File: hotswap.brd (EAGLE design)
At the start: 160 x 100 mm, 10 parts, among them U1 LTC4416EMS#PBF, U2 641737-1, U3 641737-1, U4 641737-1

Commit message: Hotswap Design Review (Asha)
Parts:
- U2: value 641737-1 -> WALL
- U3: value 641737-1 -> BATTERY
- U4: value 641737-1 -> COMPUTER
- moved R2E 5.08 mm to (25.4, 29.2)
- moved R2A 2.54 mm to (26.7, 34.3)
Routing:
- net N$9: track 15.1 -> 7.55 mm
- net N$2: track 15.8 -> 9.46 mm
- net VCC_WALL: track 21.7 -> 18.9 mm
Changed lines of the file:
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@@
 </autorouter>
 <elements>
-<element name="R2A" library="rcl" library_urn="urn:adsk.eagle:library:334" package="R0603" package3d_urn="urn:adsk.eagle:package:23555/2" value="158k" x="24.13" y="34.29" smashed="yes" rot="R90">
-<attribute name="NAME" x="23.495" y="33.655" size="1.27" layer="25" rot="R90"/>
-<attribute name="SPICEPREFIX" value="R" x="153.67" y="69.85" size="1.778" layer="27" rot="R90" display="off"/>
-<attribute name="VALUE" x="26.035" y="33.655" size="1.27" layer="27" rot="R90"/>
+<element name="R2A" library="rcl" library_urn="urn:adsk.eagle:library:334" package="R0603" package3d_urn="urn:adsk.eagle:package:23555/2" value="158k" x="26.67" y="34.29" smashed="yes" rot="R90">
+<attribute name="NAME" x="26.035" y="33.655" size="1.27" layer="25" rot="R90"/>
+<attribute name="SPICEPREFIX" value="R" x="156.21" y="69.85" size="1.778" layer="27" rot="R90" display="off"/>
+<attribute name="VALUE" x="28.575" y="33.655" size="1.27" layer="27" rot="R90"/>
 </element>
 <element name="R2C" library="rcl" library_urn="urn:adsk.eagle:library:334" package="R0603" package3d_urn="urn:adsk.eagle:package:23555/2" value="11.5k" x="27.94" y="29.21" smashed="yes" rot="R90">
@@
 <attribute name="VALUE" x="29.845" y="28.575" size="1.27" layer="27" rot="R90"/>
 </element>
-<element name="R2E" library="rcl" library_urn="urn:adsk.eagle:library:334" package="R0603" package3d_urn="urn:adsk.eagle:package:23555/2" value="105k" x="20.32" y="29.21" smashed="yes" rot="R90">
-<attribute name="NAME" x="19.685" y="28.575" size="1.27" layer="25" rot="R90"/>
-<attribute name="SPICEPREFIX" value="R" x="149.86" y="71.12" size="1.778" layer="27" rot="R90" display="off"/>
-<attribute name="VALUE" x="22.225" y="28.575" size="1.27" layer="27" rot="R90"/>
+<element name="R2E" library="rcl" library_urn="urn:adsk.eagle:library:334" package="R0603" package3d_urn="urn:adsk.eagle:package:23555/2" value="105k" x="25.4" y="29.21" smashed="yes" rot="R90">
+<attribute name="NAME" x="24.765" y="28.575" size="1.27" layer="25" rot="R90"/>
+<attribute name="SPICEPREFIX" value="R" x="154.94" y="71.12" size="1.778" layer="27" rot="R90" display="off"/>
+<attribute name="VALUE" x="27.305" y="28.575" size="1.27" layer="27" rot="R90"/>
 </element>
 <element name="U$3" library="IGVC-Discrete" package="DPACK_2" value="SUP75P03_07" x="31.75" y="43.18" smashed="yes" rot="R270">
@@
 <attribute name="VALUE" x="30.1371" y="28.639540625" size="0.4" layer="27" align="top-left"/>
 </element>
-<element name="U2" library="IGVC-Connector" package="641737-1" value="641737-1" x="13.97" y="35.56" smashed="yes" rot="R270">
+<element name="U2" library="IGVC-Connector" package="641737-1" value="WALL" x="13.97" y="35.56" smashed="yes" rot="R270">
 <attribute name="MANUFACTURER_PART_NUMBER" value="6417371" x="-16.51" y="10.16" size="1.778" layer="27" rot="R270" display="off"/>
 <attribute name="NAME" x="13.335" y="46.4566" size="1.27" layer="25" ratio="6" rot="SR270"/>
 <attribute name="VENDOR" value="TE Connectivity" x="-16.51" y="10.16" size="1.778" layer="27" rot="R270" display="off"/>
 </element>
-<element name="U3" library="IGVC-Connector" package="641737-1" value="641737-1" x="13.97" y="8.89" smashed="yes" rot="R270">
+<element name="U3" library="IGVC-Connector" package="641737-1" value="BATTERY" x="13.97" y="8.89" smashed="yes" rot="R270">
 <attribute name="MANUFACTURER_PART_NUMBER" value="6417371" x="-58.42" y="-16.51" size="1.778" layer="27" rot="R270" display="off"/>
 <attribute name="NAME" x="13.335" y="19.7866" size="1.27" layer="25" ratio="6" rot="SR270"/>
 <attribute name="VENDOR" value="TE Connectivity" x="-58.42" y="-16.51" size="1.778" layer="27" rot="R270" display="off"/>
 </element>
-<element name="U4" library="IGVC-Connector" package="641737-1" value="641737-1" x="45.72" y="36.83" smashed="yes" rot="R90">
+<element name="U4" library="IGVC-Connector" package="641737-1" value="COMPUTER" x="45.72" y="36.83" smashed="yes" rot="R90">
 <attribute name="MANUFACTURER_PART_NUMBER" value="6417371" x="160.02" y="62.23" size="1.778" layer="27" rot="R90" display="off"/>
 <attribute name="NAME" x="46.355" y="25.9334" size="1.27" layer="25" ratio="6" rot="SR90"/>
@@
 <contactref element="U1" pad="3"/>
 <contactref element="R2C" pad="1"/>
-<contactref element="U2" pad="3"/>
-<contactref element="U2" pad="4"/>
-<contactref element="U4" pad="3"/>
-<contactref element="U4" pad="4"/>
-<contactref element="U3" pad="3"/>
-<contactref element="U3" pad="4"/>
-<polygon width="0.254" layer="16">
+<polygon width="0.254" layer="16" thermals="no">
 <vertex x="0" y="58.42"/>
 <vertex x="59.69" y="58.42"/>
@@
 <wire x1="32.639" y1="30.48" x2="30.8356" y2="30.48" width="0.254" layer="1"/>
 <via x="33.02" y="30.099" extent="1-16" drill="0.35"/>
+<contactref element="U2" pad="4"/>
+<contactref element="U2" pad="3"/>
+<contactref element="U3" pad="4"/>
+<contactref element="U3" pad="3"/>
+<contactref element="U4" pad="3"/>
+<contactref element="U4" pad="4"/>
 </signal>
 <signal name="N$4">
@@
 <contactref element="U1" pad="5"/>
 <contactref element="R2E" pad="1"/>
-<wire x1="30.8356" y1="29.479240625" x2="29.21" y2="27.853640625" width="0.254" layer="1"/>
-<wire x1="29.21" y1="27.853640625" x2="29.21" y2="26.67" width="0.254" layer="1"/>
-<wire x1="29.21" y1="26.67" x2="27.94" y2="25.4" width="0.254" layer="1"/>
-<wire x1="27.94" y1="25.4" x2="21.59" y2="25.4" width="0.254" layer="1"/>
-<wire x1="21.59" y1="25.4" x2="20.32" y2="26.67" width="0.254" layer="1"/>
-<wire x1="20.32" y1="26.67" x2="20.32" y2="28.36" width="0.254" layer="1"/>
+<wire x1="30.8356" y1="29.479240625" x2="28.026359375" y2="26.67" width="0.254" layer="1"/>
+<wire x1="28.026359375" y1="26.67" x2="26.67" y2="26.67" width="0.254" layer="1"/>
+<wire x1="26.67" y1="26.67" x2="25.4" y2="27.94" width="0.254" layer="1"/>
+<wire x1="25.4" y1="27.94" x2="25.4" y2="28.36" width="0.254" layer="1"/>
 </signal>
 <signal name="N$2">
@@
 <contactref element="R2A" pad="1"/>
 <contactref element="R2C" pad="2"/>
-<wire x1="24.13" y1="33.44" x2="20.75" y2="30.06" width="0.254" layer="1"/>
-<wire x1="20.75" y1="30.06" x2="20.32" y2="30.06" width="0.254" layer="1"/>
+<wire x1="26.67" y1="33.44" x2="26.67" y2="31.33" width="0.254" layer="1"/>
+<wire x1="26.67" y1="31.33" x2="25.4" y2="30.06" width="0.254" layer="1"/>
 <wire x1="30.8356" y1="29.97961875" x2="27.94" y2="29.97961875" width="0.254" layer="1"/>
 <wire x1="27.94" y1="29.97961875" x2="27.94" y2="30.06" width="0.254" layer="1"/>
-<wire x1="20.32" y1="30.06" x2="27.85961875" y2="30.06" width="0.254" layer="1"/>
+<wire x1="25.4" y1="30.06" x2="27.85961875" y2="30.06" width="0.254" layer="1"/>
 <wire x1="27.85961875" y1="30.06" x2="27.94" y2="29.97961875" width="0.254" layer="1"/>
 </signal>
@@
 <contactref element="U2" pad="2"/>
 <contactref element="U2" pad="1"/>
-<polygon width="0.254" layer="1">
+<polygon width="0.254" layer="1" thermals="no">
 <vertex x="1.27" y="57.15"/>
 <vertex x="29.21" y="57.15"/>
@@
 <vertex x="1.27" y="41.91"/>
 </polygon>
-<wire x1="24.13" y1="35.14" x2="28.28961875" y2="30.98038125" width="0.254" layer="1"/>
-<wire x1="28.28961875" y1="30.98038125" x2="30.8356" y2="30.98038125" width="0.254" layer="1"/>
-<wire x1="24.13" y1="35.14" x2="26.95" y2="37.96" width="0.254" layer="1"/>
-<wire x1="26.95" y1="37.96" x2="26.95" y2="40.9" width="0.254" layer="1"/>
+<wire x1="26.67" y1="35.14" x2="26.88" y2="35.35" width="0.254" layer="1"/>
+<wire x1="26.88" y1="35.35" x2="26.95" y2="35.42" width="0.254" layer="1"/>
+<wire x1="26.95" y1="35.42" x2="26.95" y2="40.9" width="0.254" layer="1"/>
 <wire x1="35.2044" y1="30.98038125" x2="36.06038125" y2="30.98038125" width="0.254" layer="1"/>
 <wire x1="36.06038125" y1="30.98038125" x2="36.83" y2="31.75" width="0.254" layer="1"/>
 <via x="36.83" y="31.75" extent="1-16" drill="0.35"/>
-<wire x1="30.8356" y1="30.98038125" x2="35.2044" y2="30.98038125" width="0.254" layer="1"/>
+<wire x1="27.94" y1="32.639" x2="27.94" y2="34.29" width="0.254" layer="1"/>
+<wire x1="27.94" y1="34.29" x2="26.88" y2="35.35" width="0.254" layer="1"/>
+<wire x1="35.2044" y1="30.98038125" x2="30.8356" y2="30.98038125" width="0.254" layer="1"/>
+<wire x1="30.8356" y1="30.98038125" x2="29.59861875" y2="30.98038125" width="0.254" layer="1"/>
+<wire x1="29.59861875" y1="30.98038125" x2="27.94" y2="32.639" width="0.254" layer="1"/>
 </signal>
 <signal name="N$1">
@@
 <contactref element="U4" pad="2"/>
 <contactref element="U4" pad="1"/>
-<polygon width="0.254" layer="1">
+<polygon width="0.254" layer="1" thermals="no">
 <vertex x="58.42" y="55.88"/>
 <vertex x="58.42" y="2.54"/>
@@
 <contactref element="U3" pad="2"/>
 <contactref element="U3" pad="1"/>
-<polygon width="0.254" layer="1">
+<polygon width="0.254" layer="1" thermals="no">
 <vertex x="1.27" y="29.21"/>
-<vertex x="19.05" y="29.21"/>
 <vertex x="24.13" y="29.21"/>
-<vertex x="24.13" y="27.94"/>
 <vertex x="24.13" y="3.81"/>
 <vertex x="1.27" y="3.81"/>

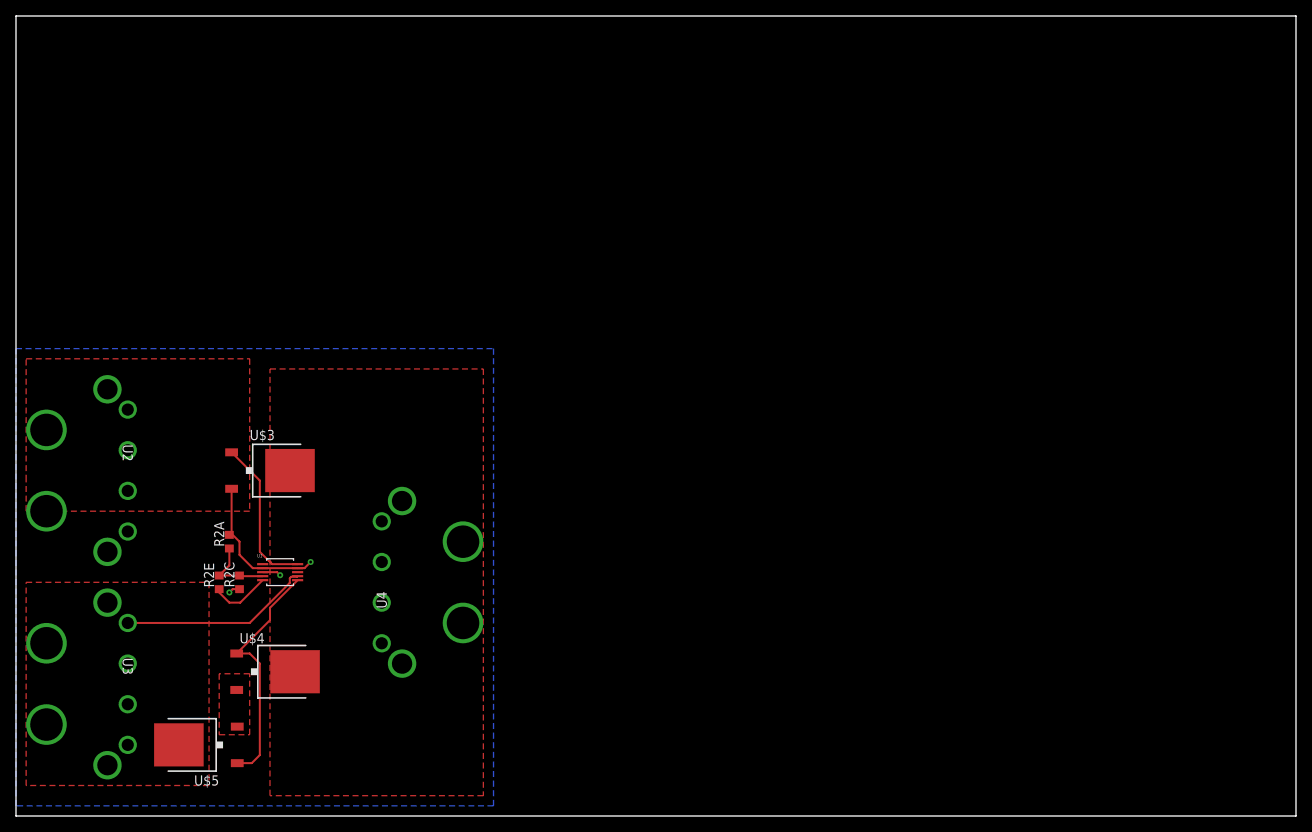
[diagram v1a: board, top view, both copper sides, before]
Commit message: fixed boundaries
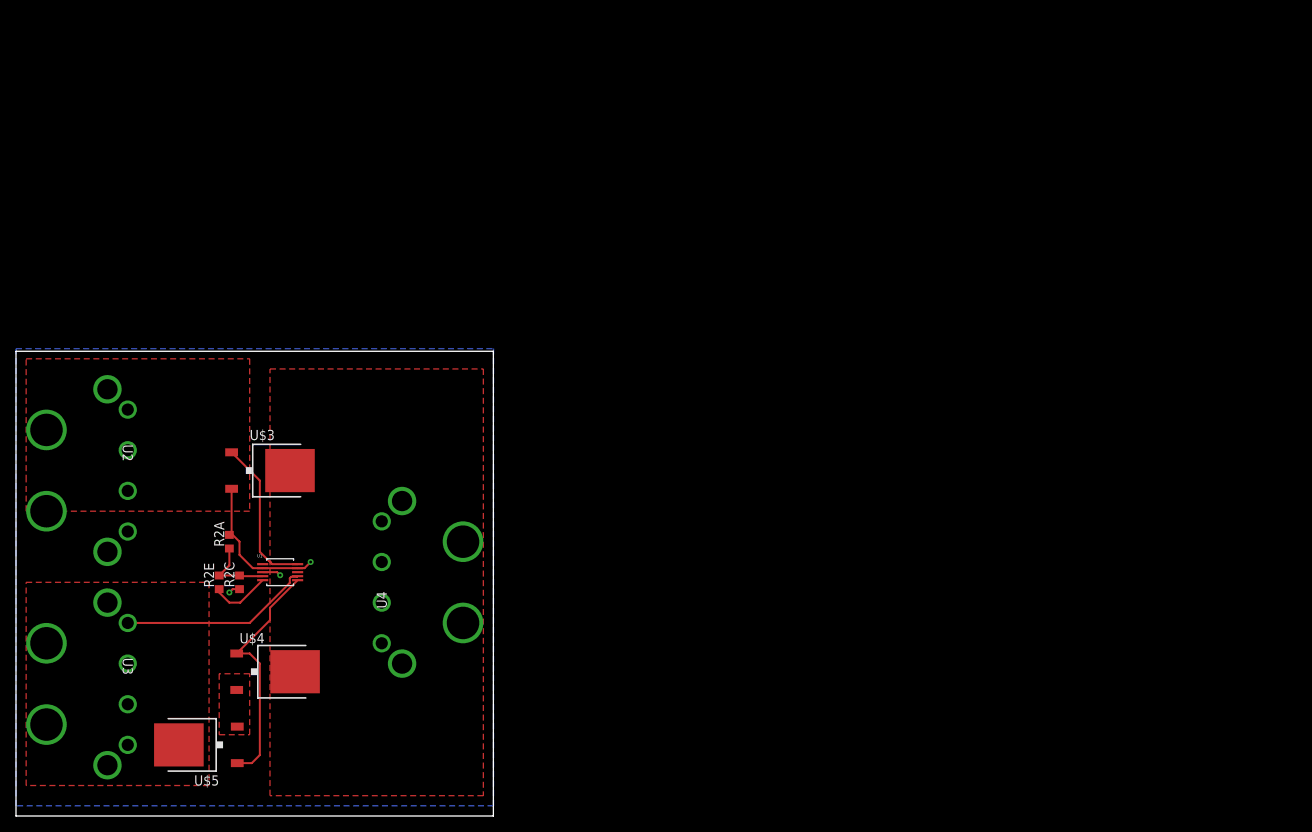
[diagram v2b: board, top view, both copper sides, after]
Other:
- board size 160 x 100 mm -> 59.7 x 58.1 mm
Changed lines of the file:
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@@
 <board>
 <plain>
-<wire x1="0" y1="0" x2="160" y2="0" width="0" layer="20"/>
-<wire x1="160" y1="0" x2="160" y2="100" width="0" layer="20"/>
-<wire x1="160" y1="100" x2="0" y2="100" width="0" layer="20"/>
-<wire x1="0" y1="100" x2="0" y2="0" width="0" layer="20"/>
+<wire x1="0" y1="0" x2="59.67" y2="0" width="0" layer="20"/>
+<wire x1="59.67" y1="0" x2="59.67" y2="58.09" width="0" layer="20"/>
+<wire x1="59.67" y1="58.09" x2="0" y2="58.09" width="0" layer="20"/>
+<wire x1="0" y1="58.09" x2="0" y2="0" width="0" layer="20"/>
 </plain>
 <attributes>
